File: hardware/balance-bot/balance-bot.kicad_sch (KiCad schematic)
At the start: 23 parts, among them J1 Conn_01x15_Socket, J10 Conn_01x02_Pin, J11 Conn_01x05_Pin, J12 Conn_01x04_Pin, J13 Conn_01x04_Pin, J2 Conn_01x15_Socket, J3 Conn_01x08_Socket, J4 Conn_01x04_Socket, J5 Conn_01x04_Socket, J6 Conn_01x03_Pin, J7 Conn_01x02_Pin, J8 Conn_01x02_Pin, J9 Conn_01x02_Pin

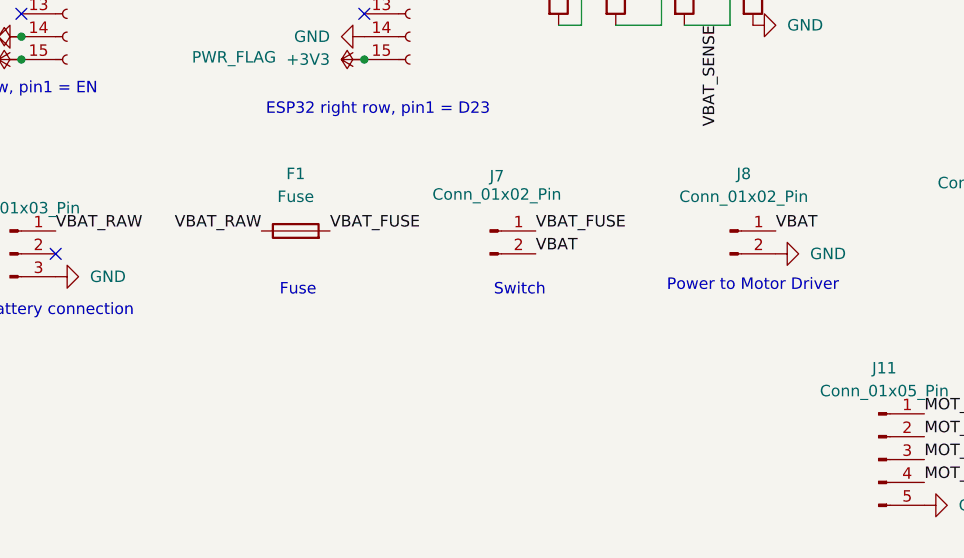
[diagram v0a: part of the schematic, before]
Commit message: Schematic: MOSFET soft power switch, fuse, buck/diode, connectors (ERC clean)
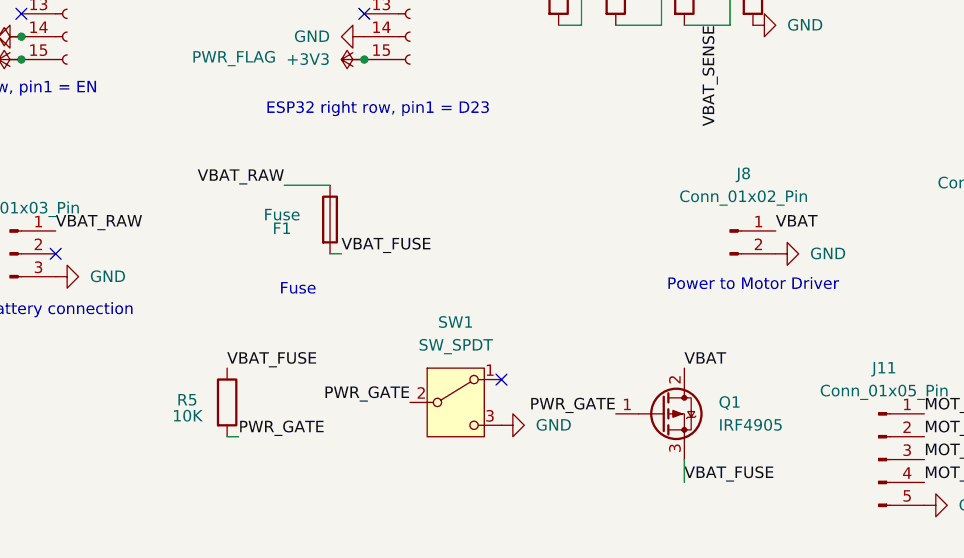
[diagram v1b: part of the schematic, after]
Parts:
- removed J7: Conn_01x02_Pin, symbol Connector:Conn_01x02_Pin
- added Q1: IRF4905, Package_TO_SOT_THT:TO-220-3_Vertical, symbol Transistor_FET:IRF4905
- added R5: 10K, symbol Device:R
- added SW1: SW_SPDT, symbol Switch:SW_SPDT
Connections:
- net GND: now also SW1.3 (C)
- net VBAT: now also Q1.2 (D)
- net VBAT_FUSE: now also Q1.3 (S), R5.1
- new net PWR_GATE: Q1.1 (G), R5.2, SW1.2 (B)
- no-connect marks 18 -> 19
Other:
- note removed: "Switch"
- moved on the sheet: F1

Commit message: Schematic complete, footprints assigned
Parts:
- D1: footprint (none) -> Diode_THT:D_DO-41_SOD81_P10.16mm_Horizontal
- F1: footprint (none) -> Fuse:Fuseholder_Cylinder-5x20mm_Schurter_0031_8201_Horizontal_Open
- H1, H2, H3, H4: footprint (none) -> MountingHole:MountingHole_3.2mm_M3
- J1, J2: footprint (none) -> Connector_PinSocket_2.54mm:PinSocket_1x15_P2.54mm_Vertical
- J10, J8, J9: footprint (none) -> Connector_JST:JST_XH_B2B-XH-A_1x02_P2.50mm_Vertical
- J11: footprint (none) -> Connector_JST:JST_XH_B5B-XH-A_1x05_P2.50mm_Vertical
- J12, J13: footprint (none) -> Connector_JST:JST_XH_B4B-XH-A_1x04_P2.50mm_Vertical
- J3: footprint (none) -> Connector_PinSocket_2.54mm:PinSocket_1x08_P2.54mm_Vertical
- J4, J5: footprint (none) -> Connector_PinSocket_2.54mm:PinSocket_1x04_P2.54mm_Vertical
- J6: footprint (none) -> Connector_JST:JST_XH_B3B-XH-A_1x03_P2.50mm_Vertical
- R1, R2, R3, R4, R5: footprint (none) -> Resistor_THT:R_Axial_DIN0207_L6.3mm_D2.5mm_P10.16mm_Horizontal
- SW1: footprint (none) -> Connector_PinHeader_2.00mm:PinHeader_1x03_P2.00mm_Vertical
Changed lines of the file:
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@@
 			)
 		)
-		(property "Footprint" ""
+		(property "Footprint" "Connector_JST:JST_XH_B4B-XH-A_1x04_P2.50mm_Vertical"
 			(at 218.44 114.3 0)
 			(effects
@@
 			)
 		)
-		(property "Footprint" ""
+		(property "Footprint" "Connector_PinSocket_2.54mm:PinSocket_1x04_P2.54mm_Vertical"
 			(at 238.76 39.37 0)
 			(effects
@@
 			)
 		)
-		(property "Footprint" ""
+		(property "Footprint" "Connector_JST:JST_XH_B3B-XH-A_1x03_P2.50mm_Vertical"
 			(at 100.33 95.25 0)
 			(effects
@@
 			)
 		)
-		(property "Footprint" ""
+		(property "Footprint" "MountingHole:MountingHole_3.2mm_M3"
 			(at 262.89 109.22 0)
 			(effects
@@
 			)
 		)
-		(property "Footprint" ""
+		(property "Footprint" "Connector_JST:JST_XH_B2B-XH-A_1x02_P2.50mm_Vertical"
 			(at 180.34 92.71 0)
 			(effects
@@
 			)
 		)
-		(property "Footprint" ""
+		(property "Footprint" "Resistor_THT:R_Axial_DIN0207_L6.3mm_D2.5mm_P10.16mm_Horizontal"
 			(at 122.682 111.76 90)
 			(effects
@@
 			)
 		)
-		(property "Footprint" ""
+		(property "Footprint" "Connector_PinHeader_2.00mm:PinHeader_1x03_P2.00mm_Vertical"
 			(at 149.86 111.76 0)
 			(effects
@@
 			)
 		)
-		(property "Footprint" ""
+		(property "Footprint" "Connector_PinSocket_2.54mm:PinSocket_1x15_P2.54mm_Vertical"
 			(at 106.68 55.88 0)
 			(effects
@@
 			)
 		)
-		(property "Footprint" ""
+		(property "Footprint" "Connector_PinSocket_2.54mm:PinSocket_1x04_P2.54mm_Vertical"
 			(at 207.01 40.64 0)
 			(effects
@@
 			)
 		)
-		(property "Footprint" ""
+		(property "Footprint" "Resistor_THT:R_Axial_DIN0207_L6.3mm_D2.5mm_P10.16mm_Horizontal"
 			(at 165.862 66.04 90)
 			(effects
@@
 			)
 		)
-		(property "Footprint" ""
+		(property "Footprint" "Connector_PinSocket_2.54mm:PinSocket_1x15_P2.54mm_Vertical"
 			(at 144.78 55.88 0)
 			(effects
@@
 			)
 		)
-		(property "Footprint" ""
+		(property "Footprint" "Resistor_THT:R_Axial_DIN0207_L6.3mm_D2.5mm_P10.16mm_Horizontal"
 			(at 181.102 66.04 90)
 			(effects
@@
 			)
 		)
-		(property "Footprint" ""
+		(property "Footprint" "Connector_PinSocket_2.54mm:PinSocket_1x08_P2.54mm_Vertical"
 			(at 181.61 45.72 0)
 			(effects
@@
 			)
 		)
-		(property "Footprint" ""
+		(property "Footprint" "MountingHole:MountingHole_3.2mm_M3"
 			(at 262.89 119.38 0)
 			(effects
@@
 			)
 		)
-		(property "Footprint" ""
+		(property "Footprint" "Diode_THT:D_DO-41_SOD81_P10.16mm_Horizontal"
 			(at 266.7 92.71 0)
 			(effects
@@
 			)
 		)
-		(property "Footprint" ""
+		(property "Footprint" "Connector_JST:JST_XH_B5B-XH-A_1x05_P2.50mm_Vertical"
 			(at 196.85 118.11 0)
 			(effects
@@
 			)
 		)
-		(property "Footprint" ""
+		(property "Footprint" "Connector_JST:JST_XH_B2B-XH-A_1x02_P2.50mm_Vertical"
 			(at 233.68 92.71 0)
 			(effects
@@
 			)
 		)
-		(property "Footprint" ""
+		(property "Footprint" "MountingHole:MountingHole_3.2mm_M3"
 			(at 262.89 114.3 0)
 			(effects
@@
 			)
 		)
-		(property "Footprint" ""
+		(property "Footprint" "Resistor_THT:R_Axial_DIN0207_L6.3mm_D2.5mm_P10.16mm_Horizontal"
 			(at 159.512 66.04 90)
 			(effects
@@
 			)
 		)
-		(property "Footprint" ""
+		(property "Footprint" "Connector_JST:JST_XH_B2B-XH-A_1x02_P2.50mm_Vertical"
 			(at 209.55 92.71 0)
 			(effects
@@
 			)
 		)
-		(property "Footprint" ""
+		(property "Footprint" "Fuse:Fuseholder_Cylinder-5x20mm_Schurter_0031_8201_Horizontal_Open"
 			(at 134.112 91.44 90)
 			(effects
@@
 			)
 		)
-		(property "Footprint" ""
+		(property "Footprint" "Resistor_THT:R_Axial_DIN0207_L6.3mm_D2.5mm_P10.16mm_Horizontal"
 			(at 173.482 66.04 90)
 			(effects
@@
 			)
 		)
-		(property "Footprint" ""
+		(property "Footprint" "Connector_JST:JST_XH_B4B-XH-A_1x04_P2.50mm_Vertical"
 			(at 240.03 114.3 0)
 			(effects
@@
 			)
 		)
-		(property "Footprint" ""
+		(property "Footprint" "MountingHole:MountingHole_3.2mm_M3"
 			(at 262.89 124.46 0)
 			(effects

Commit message: PCB v1.0: complete layout and routing
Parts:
- removed J10, J9: Conn_01x02_Pin, Connector_JST:JST_XH_B2B-XH-A_1x02_P2.50mm_Vertical, symbol Connector:Conn_01x02_Pin
- added J7: Conn_01x04_Socket, balance-bot:Buck_LM2596, symbol Connector:Conn_01x04_Socket
- added J9: Conn_01x06_Pin, Connector_JST:JST_XH_B6B-XH-A_1x06_P2.50mm_Vertical, symbol Connector:Conn_01x06_Pin
- D1: value D_Schottky -> 1N4001
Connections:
- net +3V3: now also J9.1 (Pin_1)
- net BUCK_5V: now also J7.3 (Pin_3)
- net ENC1_A: now also J1.13 (Pin_13); no longer J2.10 (Pin_10)
- net ENC1_B: now also J1.10 (Pin_10); no longer J2.7 (Pin_7)
- net ENC2_A: now also J2.10 (Pin_10); no longer J2.9 (Pin_9)
- net GND: now also J7.2 (Pin_2), J7.4 (Pin_4), J9.2 (Pin_2)
- net SCL: now also J9.4 (Pin_4)
- net SDA: now also J9.3 (Pin_3)
- net VBAT: now also J7.1 (Pin_1)
- new net TOF_INT: J2.9 (Pin_9), J9.6 (Pin_6)
- new net TOF_XSHUT: J2.7 (Pin_7), J9.5 (Pin_5)
- no-connect marks 19 -> 17
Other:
- note added: "Buck"
- note removed: "Buck In"
- note removed: "Buck Out"
